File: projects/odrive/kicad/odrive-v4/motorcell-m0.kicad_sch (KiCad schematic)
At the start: 57 parts, among them J2 M0 A/B/C, Q10 NVMFS5C628NL, Q11 NVMFS5C628NL, Q12 NVMFS5C628NL, Q13 NVMFS5C628NL, Q14 NVMFS5C628NL, Q15 NVMFS5C628NL, Q16 NVMFS5C628NL, Q17 NVMFS5C628NL, Q18 NVMFS5C628NL, Q19 NVMFS5C628NL, Q20 NVMFS5C628NL, Q21 NVMFS5C628NL, U3 DRV8353RS

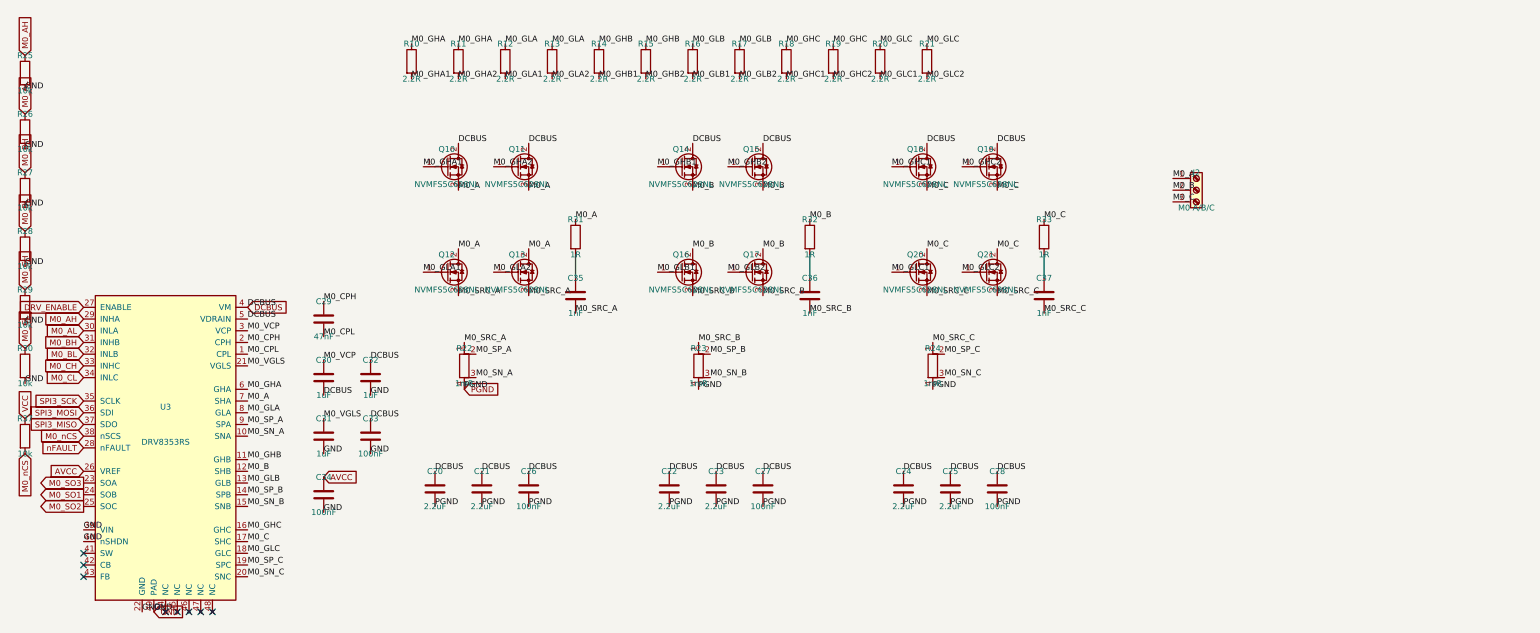
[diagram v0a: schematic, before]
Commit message: Make the v4 schematic sheets readable, netlist-invariant
The verified v4 schematic was electrically perfect and visually unreadable:
connectivity lived in labels stuck on pins, text overlapped, and parts sat
on the title block. Reworked all ten block sheets through Konnect: real
wires for local connections, labels kept for power rails and inter-sheet
nets, parts grouped by function, junction dots where wires join.

The invariant was enforced, not assumed: the exported netlist is diffed
against a reference frozen before the rework - 378 components and 283 nets,
identical membership pin by pin - and ERC holds at 0 errors. The lesson
that forced the rework is now a standing gate: numeric oracles (ERC,
netlist diff, overlap counts) all passed on the unreadable version, so
every sheet is also rendered to PNG and looked at before being declared
done.

An interrupted fix round left one known cosmetic issue, documented in
docs/LOG.md: the encoders-gpio GPIO group's reference/value text fields
float ~134mm right of their symbols, over the title block. konnect 0.2.2
has no tool that repositions property fields, so it waits for 0.11.0.
Also adds the fab footprints the sheets reference (MEGA fuse, Phoenix
terminal blocks, CMC) and restores the board file to the blank template -
the aborted layout skeleton was not worth keeping.
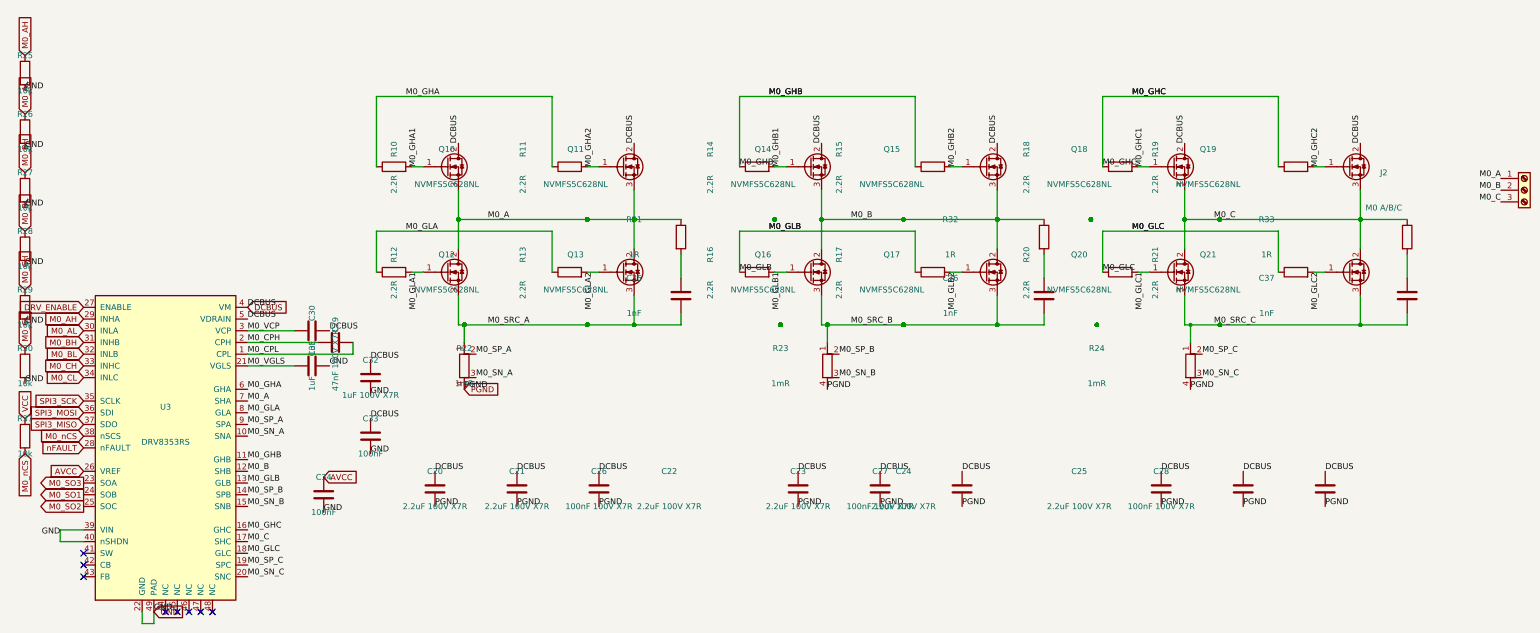
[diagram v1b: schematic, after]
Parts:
- C20, C21, C22, C23, C24, C25: value 2.2uF -> 2.2uF 100V X7R; footprint (none) -> Capacitor_SMD:C_1210_3225Metric
- C26, C27, C28: value 100nF -> 100nF 100V X7R; footprint (none) -> Capacitor_SMD:C_0603_1608Metric
- C29: value 47nF -> 47nF 100V X7R; footprint (none) -> Capacitor_SMD:C_0805_2012Metric
- C30, C31, C33, C34, C35, C36, C37: footprint (none) -> Capacitor_SMD:C_0603_1608Metric
- C32: value 1uF -> 1uF 100V X7R; footprint (none) -> Capacitor_SMD:C_1210_3225Metric
- J2: footprint (none) -> odrive_footprints:TerminalBlock_Phoenix_PC-16-3-ST-10.16mm
- Q10, Q11, Q12, Q13, Q14, Q15, Q16, Q17, Q18, Q19, Q20, Q21: footprint (none) -> Package_SO:PowerPAK_SO-8_Single
- R10, R11, R12, R13, R14, R15, R16, R17, R18, R19, R20, R21, R25, R26, R27, R28, R29, R30, R31, R32, R33, R37: footprint (none) -> Resistor_SMD:R_0603_1608Metric
- R22, R23, R24: footprint (none) -> Resistor_SMD:R_Shunt_Vishay_WSK2512_6332Metric_T1_T2
- U3: footprint (none) -> Package_DFN_QFN:QFN-48-1EP_7x7mm_P0.5mm_EP5.15x5.15mm_ThermalVias
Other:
- moved on the sheet: C21, C22, C23, C24, C25, C26, C27, C28, C29, C30, C31, C35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
